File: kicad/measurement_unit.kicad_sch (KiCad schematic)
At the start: 18 parts, among them U401 74LVC1G02W5, U402 74LVC1G80GW, U403 74HC04PW, U404 74LVC1G80GW, U405 74VHC4040FT, U406 74VHC4040FT, U407 74VHC4040FT

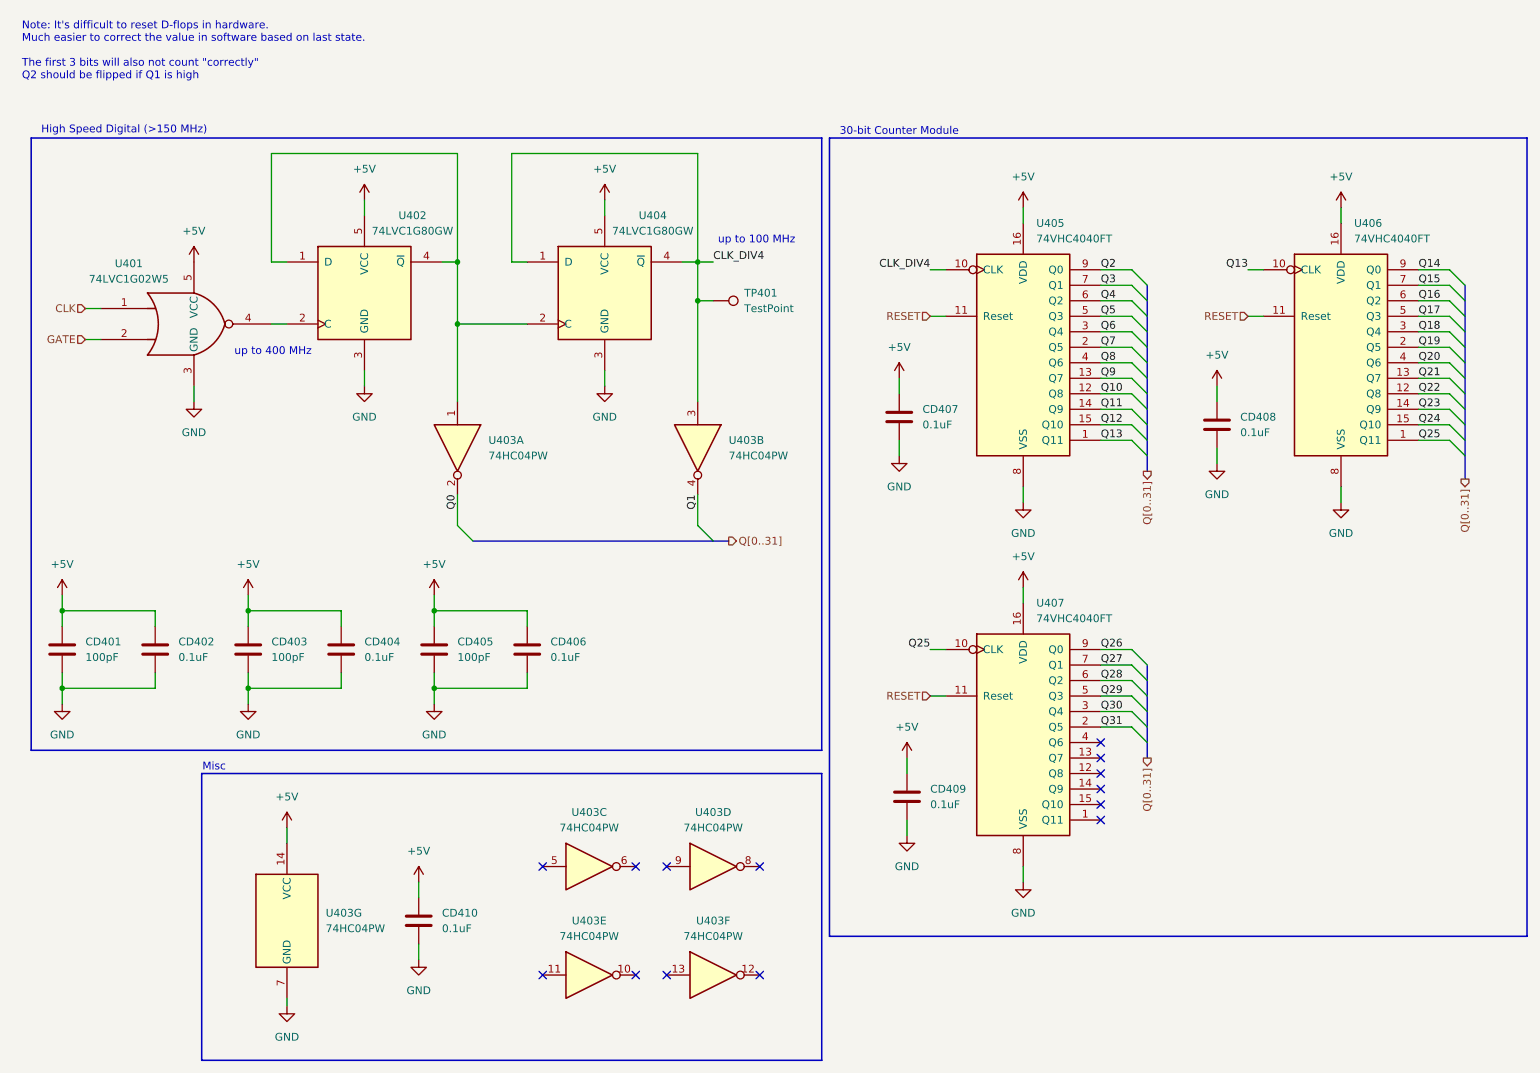
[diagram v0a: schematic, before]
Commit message: rework isp header, update pinout
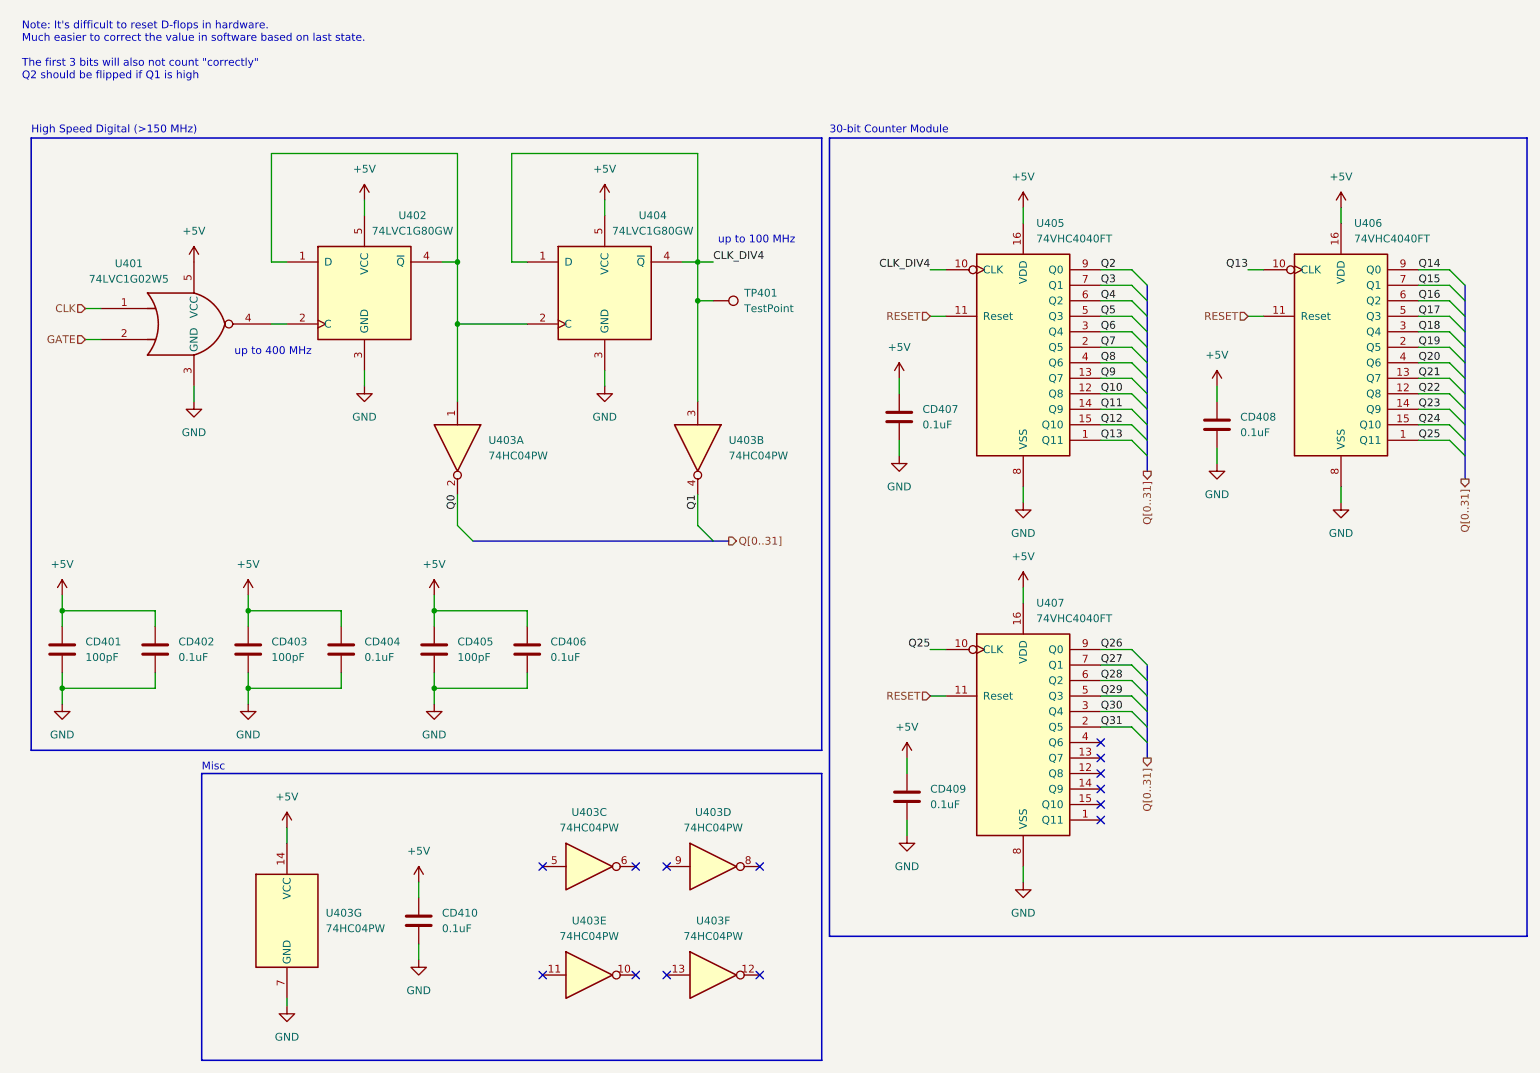
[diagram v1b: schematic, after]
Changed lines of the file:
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@@
 	(title_block
 		(title "Frequency Counter")
-		(date "2025-11-19")
-		(rev "1.0")
+		(date "2025-12-25")
+		(rev "2.0-draft")
 		(company "vladaviedov.org")
 		(comment 1 "Maximum Precision (125 mHz ~ 325 MHz): 62.5 mHz")
@@
 	(text "High Speed Digital (>150 MHz)"
 		(exclude_from_sim no)
-		(at 31.75 33.02 0)
+		(at 16.51 33.02 0)
 		(effects
 			(font
 				(size 1.27 1.27)
 			)
+			(justify left)
 		)
 	)
 	(text "Misc"
 		(exclude_from_sim no)
-		(at 46.482 137.414 0)
+		(at 44.45 137.414 0)
 		(effects
 			(font
 				(size 1.27 1.27)
 			)
+			(justify left)
 		)
 	)
@@
 	(text "30-bit Counter Module"
 		(exclude_from_sim no)
-		(at 158.75 33.274 0)
+		(at 147.32 33.02 0)
 		(effects
 			(font
 				(size 1.27 1.27)
 			)
+			(justify left)
 		)
 	)

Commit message: split frontend into two channels
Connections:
- net CLK renamed CLK_A
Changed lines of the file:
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@@
 	(title_block
 		(title "Frequency Counter")
-		(date "2025-12-25")
+		(date "2026-02-17")
 		(rev "2.0-draft")
 		(company "vladaviedov.org")
@@
 		)
 	)
+	(hierarchical_label "CH_SEL"
+		(shape input)
+		(at 118.11 25.4 180)
+		(effects
+			(font
+				(size 1.27 1.27)
+			)
+			(justify right)
+		)
+	)
 	(hierarchical_label "GATE"
 		(shape input)
@@
 		)
 	)
-	(hierarchical_label "CLK"
+	(hierarchical_label "CLK_B"
+		(shape input)
+		(at 118.11 22.86 180)
+		(effects
+			(font
+				(size 1.27 1.27)
+			)
+			(justify right)
+		)
+	)
+	(hierarchical_label "CLK_A"
 		(shape input)
 		(at 25.4 62.23 180)

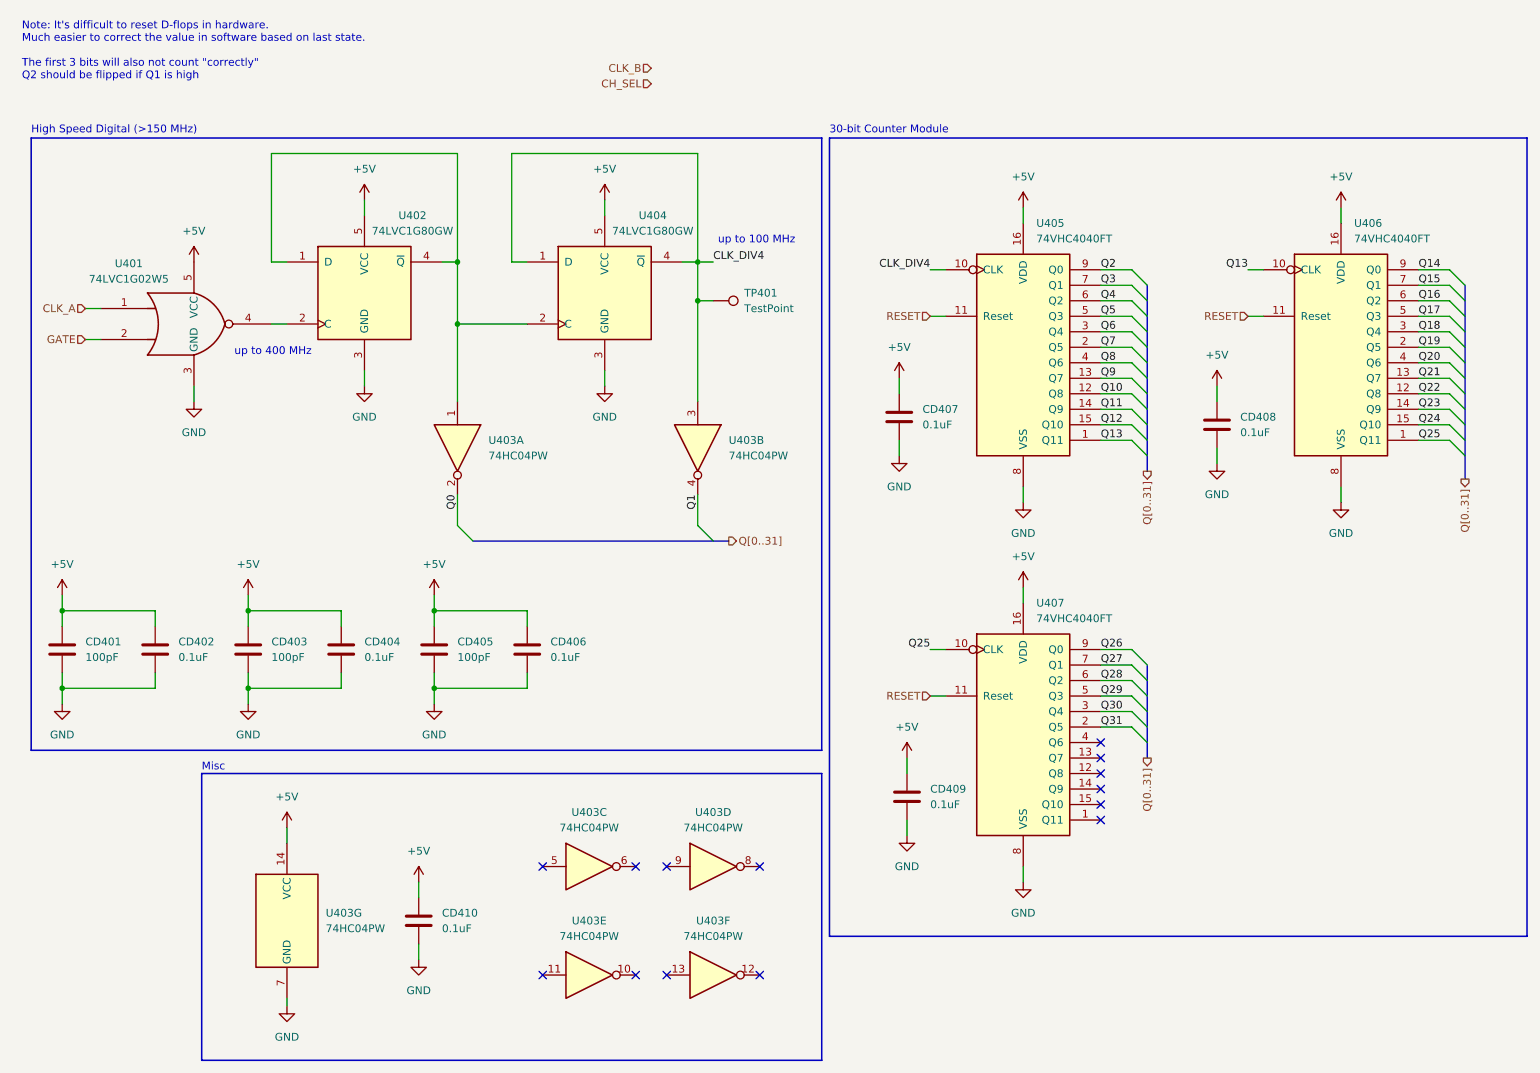
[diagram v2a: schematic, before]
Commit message: rework frontend, channel gating
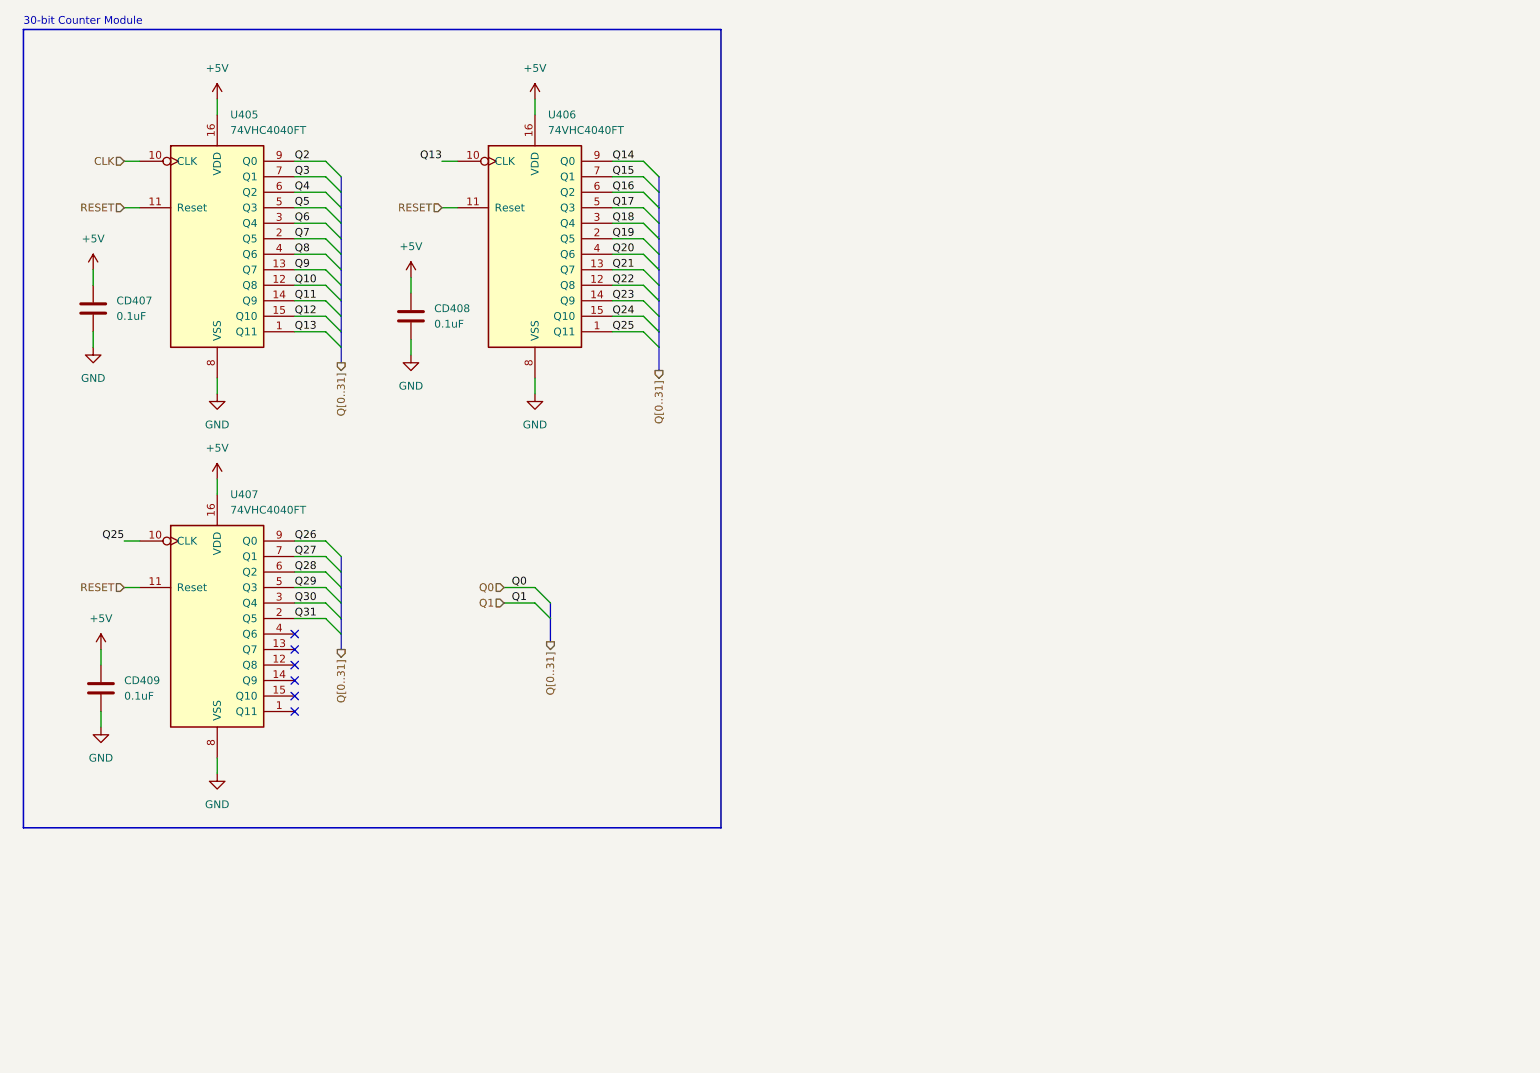
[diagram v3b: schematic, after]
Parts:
- removed CD401, CD403, CD405: 100pF, Custom:C_0402_1005Metric_Fix, symbol Device:C
- removed CD402, CD404, CD406, CD410: 0.1uF, Custom:C_0402_1005Metric_Fix, symbol Device:C
- removed TP401: TestPoint, Custom:TestPoint_Pad_2.0x2.0mm_Fix, symbol Connector:TestPoint
- removed U401: 74LVC1G02W5, Package_TO_SOT_SMD:SC-74A-5_1.55x2.9mm_P0.95mm, symbol 74xGxx:74LVC1G02
- removed U402, U404: 74LVC1G80GW, Package_TO_SOT_SMD:SOT-353_SC-70-5, symbol 74xGxx:74LVC1G80
- removed U403: 74HC04PW, Package_SO:TSSOP-14_4.4x5mm_P0.65mm, symbol 74xx:74HC04
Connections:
- net CLK_DIV4 renamed CLK
- no-connect marks 14 -> 6
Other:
- note removed: "High Speed Digital (>150 MHz)"
- note removed: "Misc"
- note removed: "Note: It's difficult to reset D-flops in hardware. Much easier to correct the value in software based on last state. The first 3 bits will also not count "correctly" Q2 should be flipped if Q1 is high"
- note removed: "up to 100 MHz"
- note removed: "up to 400 MHz"
- moved on the sheet: CD407, CD408, CD409, U405, U406, U407

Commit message: replace alum caps with ceramics, change mpn labeling
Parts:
- CD407, CD408, CD409: MPN (none) -> KGM05AR51C104KH; Supplier https://www.digikey.com/en/products/detail/kyocera-avx/KGM0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 -> (none)
- U405, U406, U407: MPN (none) -> 74VHC4040FT; Supplier https://www.digikey.com/en/products/detail/toshiba-semicond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 -> (none)
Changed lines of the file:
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@@
 			)
 		)
-		(property "Supplier" "https://www.digikey.com/en/products/detail/kyocera-avx/KGM05AR51C104KH/563236"
+		(property "Supplier" ""
+			(at 26.67 62.23 0)
+			(effects
+				(font
+					(size 1.27 1.27)
+				)
+				(hide yes)
+			)
+		)
+		(property "MPN" "KGM05AR51C104KH"
 			(at 26.67 62.23 0)
 			(effects
@@
 			)
 		)
-		(property "Supplier" "https://www.digikey.com/en/products/detail/toshiba-semiconductor-and-storage/74VHC4040FT/5155784"
+		(property "Supplier" ""
+			(at 46.99 50.8 0)
+			(effects
+				(font
+					(size 1.27 1.27)
+				)
+				(hide yes)
+			)
+		)
+		(property "MPN" "74VHC4040FT"
 			(at 46.99 50.8 0)
 			(effects
@@
 			)
 		)
-		(property "Supplier" "https://www.digikey.com/en/products/detail/kyocera-avx/KGM05AR51C104KH/563236"
+		(property "Supplier" ""
+			(at 27.94 124.46 0)
+			(effects
+				(font
+					(size 1.27 1.27)
+				)
+				(hide yes)
+			)
+		)
+		(property "MPN" "KGM05AR51C104KH"
 			(at 27.94 124.46 0)
 			(effects
@@
 			)
 		)
-		(property "Supplier" "https://www.digikey.com/en/products/detail/toshiba-semiconductor-and-storage/74VHC4040FT/5155784"
+		(property "Supplier" ""
+			(at 99.06 50.8 0)
+			(effects
+				(font
+					(size 1.27 1.27)
+				)
+				(hide yes)
+			)
+		)
+		(property "MPN" "74VHC4040FT"
 			(at 99.06 50.8 0)
 			(effects
@@
 			)
 		)
-		(property "Supplier" "https://www.digikey.com/en/products/detail/toshiba-semiconductor-and-storage/74VHC4040FT/5155784"
+		(property "Supplier" ""
+			(at 46.99 113.03 0)
+			(effects
+				(font
+					(size 1.27 1.27)
+				)
+				(hide yes)
+			)
+		)
+		(property "MPN" "74VHC4040FT"
 			(at 46.99 113.03 0)
 			(effects
@@
 			)
 		)
-		(property "Supplier" "https://www.digikey.com/en/products/detail/kyocera-avx/KGM05AR51C104KH/563236"
+		(property "Supplier" ""
 			(at 78.74 63.5 0)
 			(effects
+				(font
+					(size 1.27 1.27)
+				)
+				(hide yes)
+			)
+		)
+		(property "MPN" "KGM05AR51C104KH"
+			(at 78.74 63.5 0)
+			(effects
